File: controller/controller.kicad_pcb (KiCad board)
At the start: 2 copper layers, 223.5 x 91.4 mm, 414 parts, among them J1 PRG, J10 PRI_TRF_L, J11 PRI_TRF_N, J12 SEC_OUT_L, J13 SEC_OUT_N, J14 Left, J15 Right, J16 Conn_01x03_Male, J17 Conn_01x03_Male, J18 ch5, J19 ch6, J2 AMP_1, J20 ch1, J21 ch2, J22 ch3, J23 ch4, J24 AMP_4, J25 AMP_5, J26 AMP_6, J27 TP, J28 TP, J29 TP, J3 BUTTON, J30 TP, J31 TP, J32 TP, J33 TP, J34 TP, J35 TP, J36 TP, J37 TP, J38 TP, J39 TP, J4 AMP_2, J40 LCD, J41 TempSens1, J42 TempSens2, J43 TP, J44 TP, J45 TP, J46 TP, J47 USB, J48 PRG, J49 AFBR-2624Z, J5 AMP_3, J6 MAIN_PWR_L, J7 MAIN_PWR_N, J8 SEC_TRF_L, J9 SEC_TRF_N, M1 Fan_4pin, M2 Fan_4pin, Q1 STD2805, Q10 BC846A, Q11 BC846A, Q12 BC847, Q13 BC847, Q2 BC846A, Q3 BC847, Q4 BC847, Q5 BC847, Q6 BC847, Q7 BC847, Q8 BC847, Q9 BC847, U1 LM2596S-ADJ, U10 ADA4807-2ARM, U11 ADA4807-2ARM, U12 ADA4807-2ARM, U13 ADA4807-2ARM, U14 ADA4807-2ARM, U15 ADA4807-2ARM, U16 ADA4807-2ARM, U17 LM1085-ADJ, U18 LM1085-ADJ, U19 TCM809, U2 ADAU1467WBCPZ300, U20 TCM809, U21 24LC64, U3 25AA1024, U4 STM32F407VETx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

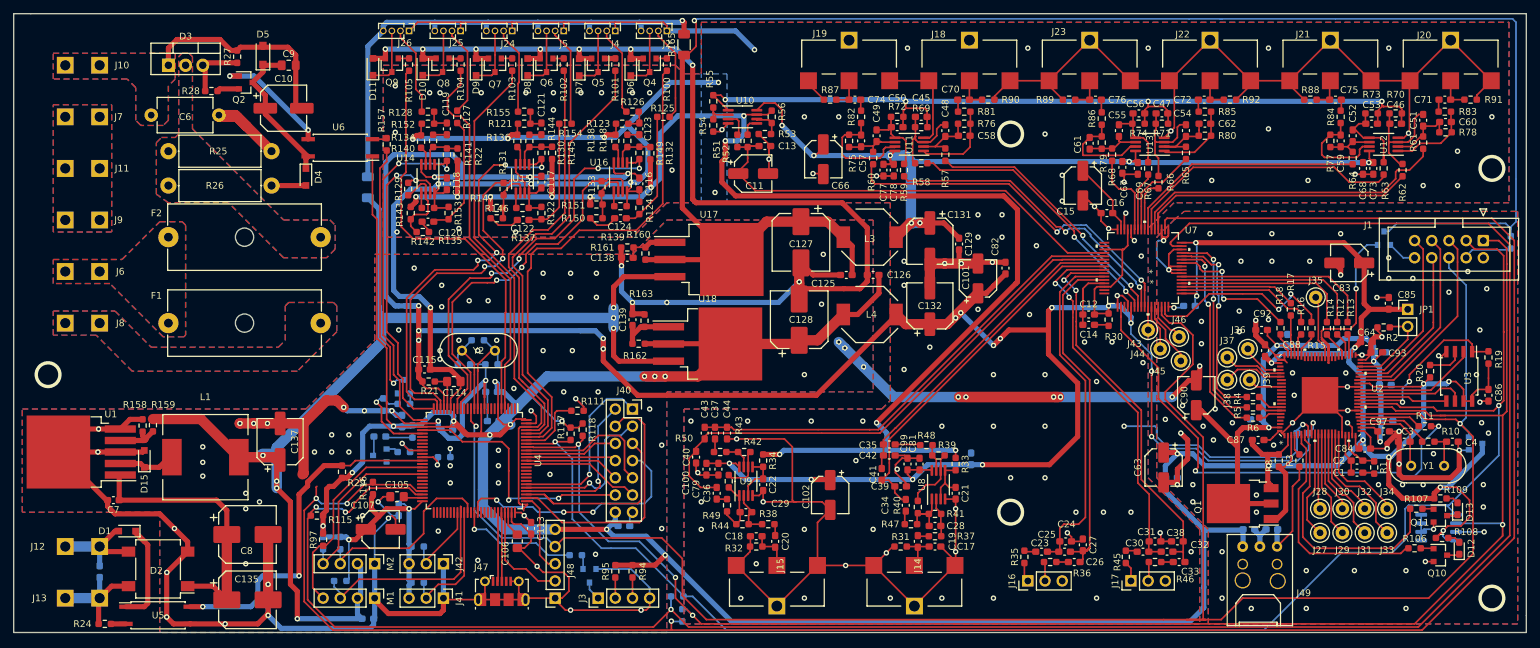
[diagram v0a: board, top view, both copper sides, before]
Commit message: update components
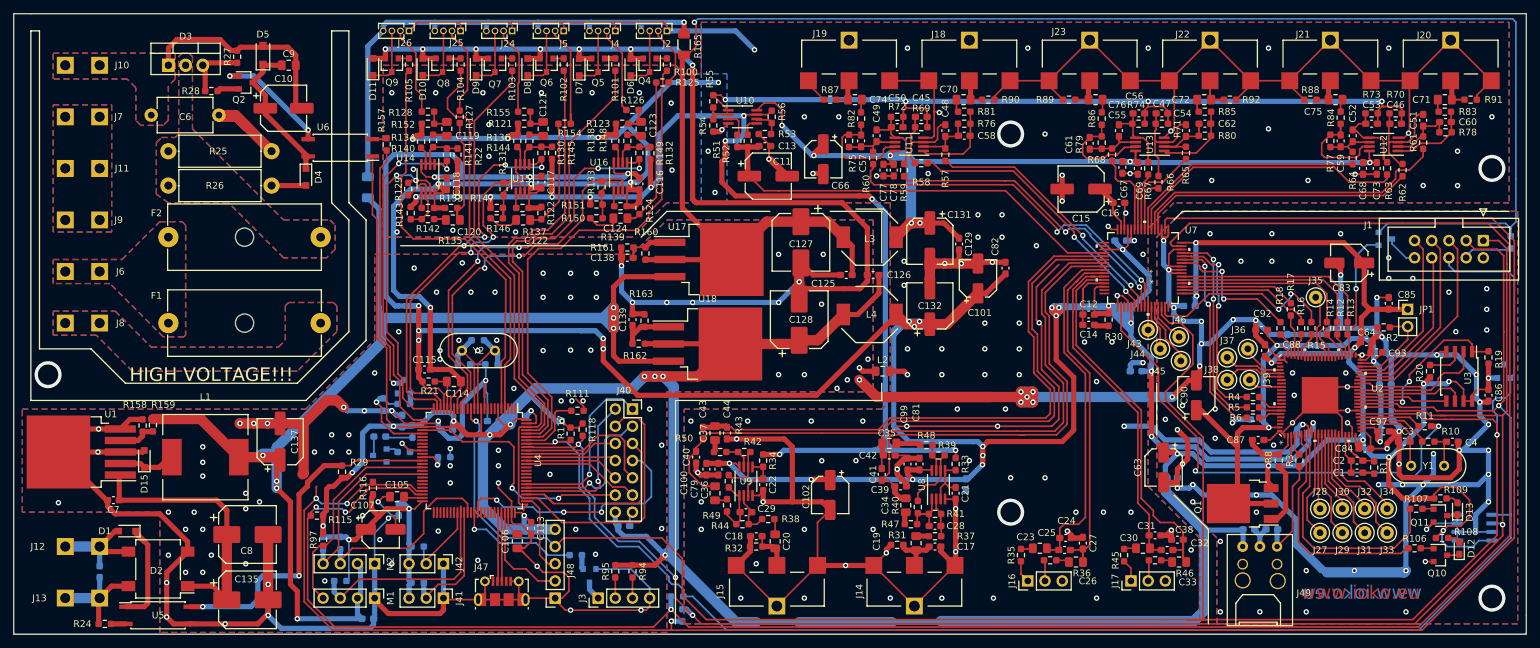
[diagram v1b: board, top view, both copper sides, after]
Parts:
- added C141: 0.1, Capacitor_SMD:C_0603_1608Metric_Pad1.08x0.95mm_HandSolder, B.Cu at (183.6, 96.0)
- added C142: 0.1, Capacitor_SMD:C_0603_1608Metric_Pad1.08x0.95mm_HandSolder, B.Cu at (181.4, 76.7)
- added L2: FB, Inductor_SMD:L_0805_2012Metric_Pad1.15x1.40mm_HandSolder, F.Cu at (146.2, 96.0)
- C105, C106, C114: footprint Resistor_SMD:R_0805_2012Metric_Pad1.20x1.40mm_HandSolder -> Capacitor_SMD:C_0805_2012Metric_Pad1.18x1.45mm_HandSolder
- C11, C15: footprint Capacitor_SMD:CP_Elec_5x5.8 -> Capacitor_SMD:CP_Elec_6.3x5.3
- C119, C120, C121, C122, C123, C124, C19, C20, C23, C30, C33, C34, C35, C36, C37, C70, C71, C72, C74, C75, C76: footprint Capacitor_SMD:C_0603_1608Metric_Pad1.08x0.95mm_HandSolder -> Capacitor_SMD:C_0805_2012Metric_Pad1.18x1.45mm_HandSolder
- C25, C32: value 10hF -> 100pF
- C26: value 10hF -> 10uF; footprint Capacitor_SMD:C_0603_1608Metric_Pad1.08x0.95mm_HandSolder -> Capacitor_SMD:C_0805_2012Metric_Pad1.18x1.45mm_HandSolder
- U19, U20: value TCM809 -> MCP130-xxxxTT
- moved U19 11.5 mm to (238.0, 96.0), turned to 90 degrees
- moved C112 5.54 mm to (92.6, 102.7), turned to 0 degrees
- moved U21 5.33 mm to (233.7, 119.1)
- moved R125 5.08 mm to (113.6, 53.3)
- moved C80 3.89 mm to (158.5, 112.8), turned to 270 degrees
- moved C120 3.69 mm to (82.7, 73.7)
- moved C16 2.34 mm to (181.1, 71.1), turned to 0 degrees
- moved C11 2.27 mm to (129.3, 67.2)
- moved R142 2.05 mm to (79.0, 73.5)
- moved C31 0.89 mm to (186.4, 120.3)
- moved R153 0.85 mm to (82.4, 71.9), turned to 0 degrees
- moved R38 0.76 mm to (129.3, 117.9)
- moved R35 0.57 mm to (166.6, 123.2)
- moved C15 0.57 mm to (175.5, 69.1), turned to 180 degrees
- moved C23 0.57 mm to (169.4, 122.2)
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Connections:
- U19 pad 1: GND -> /codec/nRST
- U19 pad 2: /codec/nRST -> +3V3
- U19 pad 3: +3V3 -> GND
- U20 pad 1: GND -> /dsp/WR_BACK
- U20 pad 2: /dsp/WR_BACK -> +5V
- U20 pad 3: +5V -> GND
- U7 pad 57: /codec/BAL_IN_L_P -> /codec/BAL_IN_R_P
- U7 pad 58: /codec/BAL_IN_L_N -> /codec/BAL_IN_R_N
- U7 pad 59: /codec/BAL_IN_R_P -> /codec/BAL_IN_L_P
- U7 pad 60: /codec/BAL_IN_R_N -> /codec/BAL_IN_L_N
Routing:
- net GND: track 739.2 -> 977.9 mm, vias 168 -> 185
- net GNDA: track 625.7 -> 763.7 mm, vias 115 -> 124
- net +3.3VA: track 461.5 -> 561.8 mm, vias 22 -> 26
- net +3V3: track 704.7 -> 791.4 mm, vias 28 -> 26
- net /codec/AMP_REF_IN: track 215.5 -> 190.7 mm
- net /codec/SE_IN_L_P: track 69.8 -> 89.5 mm
- net /codec/SE_IN_R_N: track 54.1 -> 73.5 mm
- net +5VA: track 167.9 -> 187.1 mm
- net /codec/SE_IN_R_P: track 47.3 -> 65.3 mm
- net /codec/nRST: track 297.9 -> 313.9 mm
- net /codec/SE_IN_L_N: track 81.4 -> 96.9 mm
- net /dsp/WR_BACK: track 31.7 -> 24.1 mm
- net +12V: track 186.8 -> 194.1 mm
- net /ucu/DSP_SDA: track 237.4 -> 244.3 mm
- net /ucu/DSP_SCL: track 248.5 -> 242.0 mm
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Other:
- board size 223.5 x 91.4 mm -> 223.5 x 91.7 mm
- board text added: "HIGH VOLTAGE!!!"
- board text added: "www.ioko.eu"

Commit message: Fix misc issues
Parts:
- added C143: 0.1, Capacitor_SMD:C_0603_1608Metric_Pad1.08x0.95mm_HandSolder, F.Cu at (219.6, 111.9)
- added NT1: NT1, NetTie:NetTie-2_SMD_Pad0.5mm, F.Cu at (220.5, 113.7)
- D14, Q12, R119: moved to F.Cu
- R158: value R -> 1K3
- R159: value R -> 11K
- R160: value R -> 360R
- R161: value R -> 1K1
- R162: value R -> 620R
- R163: value R -> 1K
- moved R120 6.27 mm to (70.5, 105.4), turned to 0 degrees
- moved Q12 3.41 mm to (70.4, 105.4), turned to 270 degrees
- moved D14 2.61 mm to (71.3, 108.2)
- moved C1 0.90 mm to (215.4, 110.9)
- moved C2 0.90 mm to (215.4, 109.3)
- moved R1 0.89 mm to (217.9, 110.2)
- moved C84 0.76 mm to (218.2, 107.4)
- moved R119 0.57 mm to (74.9, 107.7)
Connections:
- C6 pad 2: Net-(C10-Pad2) -> Net-(C6-Pad2)
- D3 pad 1: Net-(C10-Pad2) -> Net-(C6-Pad2)
- J10 pad 1: Net-(C10-Pad2) -> Net-(C6-Pad2)
- J11 pad 1: Net-(J11-Pad1) -> Net-(C10-Pad2)
- J7 pad 1: Net-(J11-Pad1) -> Net-(C10-Pad2)
- J9 pad 1: Net-(J11-Pad1) -> Net-(C10-Pad2)
- U4 pad 84: (no net) -> /ucu/PON
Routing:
- net /ucu/PON: track 3.05 -> 38.4 mm, vias 0 -> 2
- net Net-(C10-Pad2): track 31.3 -> 63.7 mm
- net /ucu/SPK_4_ON: track 75.7 -> 61.8 mm
- net GND: track 977.9 -> 987.9 mm, vias 185 -> 187
- net VPP: track 5.90 -> 15.5 mm
- net Net-(R119-Pad2): track 5.18 -> 2.34 mm, vias 1 -> 0
- net Net-(Q12-Pad1): track 1.83 -> 4.61 mm
- net Net-(R132-Pad2): track 62.5 -> 59.8 mm
- net /ucu/CODEC_SCL: track 323.1 -> 321.4 mm
- net Net-(R133-Pad2): track 55.7 -> 54.5 mm
- net Net-(D14-Pad1): track 2.85 -> 1.81 mm
- net +3V3: track 791.4 -> 792.5 mm
- net Net-(D14-Pad2): track 4.01 -> 3.11 mm, vias 0 -> 1
- net /ucu/SPK_1_ON: track 74.0 -> 73.1 mm
- net Net-(C2-Pad1): track 6.80 -> 6.09 mm
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- added copper zone on F.Cu, net +3V3
- added copper zone on B.Cu, net Net-(C6-Pad2)
- added copper zone on F.Cu, net Net-(C6-Pad2)
- removed copper zone on B.Cu, net Net-(J11-Pad1)
- removed copper zone on F.Cu, net Net-(J11-Pad1)
